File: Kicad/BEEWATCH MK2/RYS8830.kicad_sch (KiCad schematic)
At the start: 33 parts, among them Q4 DMG6968U, Q5 BSS138, Q6 BSS138, Q7 BSS138, Q8 DMP1045U-7, U2 LTC3549EDCB#TRMPBF, U7 RYS8830

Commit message: Changed +3V3 to +3.3V
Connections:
- net +3V3 renamed +3.3V
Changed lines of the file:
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@@
-	)
-	(symbol
-		(lib_id "power:+5V")
-		(at 228.6 100.33 0)
-		(mirror x)
-		(unit 1)
-		(exclude_from_sim no)
-		(in_bom yes)
-		(on_board yes)
-		(dnp no)
-		(property "Reference" "#PWR068"
-			(at 228.6 96.52 0)
-			(effects
-				(font
-					(size 1.27 1.27)
-				)
-				(hide yes)
-			)
-		)
-		(property "Value" "+3V3"
-			(at 228.6 105.41 0)
-			(effects
-				(font
-					(size 1.27 1.27)
-				)
-			)
-		)
-		(property "Footprint" ""
-			(at 228.6 100.33 0)
-			(effects
-				(font
-					(size 1.27 1.27)
-				)
-				(hide yes)
-			)
-		)
-		(property "Datasheet" ""
-			(at 228.6 100.33 0)
-			(effects
-				(font
-					(size 1.27 1.27)
-				)
-				(hide yes)
-			)
-		)
-		(property "Description" "Power symbol creates a global label with name \"+5V\""
-			(at 228.6 100.33 0)
-			(effects
-				(font
-					(size 1.27 1.27)
-				)
-				(hide yes)
-			)
-		)
-		(pin "1"
-		)
-		(instances
-			(project "BEEWATCH MK3"
-				(path "/e9c5fb53-480b-4989-8495-a3341ee99514/33dec73c-f7ec-4dd7-9d85-ef473e07baa9"
-					(reference "#PWR068")
-					(unit 1)
-				)
-			)
-		)
 	)
 	(symbol
@@
 	)
 	(symbol
+		(lib_id "power:+5V")
+		(at 229.87 152.4 180)
+		(unit 1)
+		(exclude_from_sim no)
+		(in_bom yes)
+		(on_board yes)
+		(dnp no)
+		(property "Reference" "#PWR087"
+			(at 229.87 148.59 0)
+			(effects
+				(font
+					(size 1.27 1.27)
+				)
+				(hide yes)
+			)
+		)
+		(property "Value" "+3.3V"
+			(at 229.87 157.48 0)
+			(effects
+				(font
+					(size 1.27 1.27)
+				)
+			)
+		)
+		(property "Footprint" ""
+			(at 229.87 152.4 0)
+			(effects
+				(font
+					(size 1.27 1.27)
+				)
+				(hide yes)
+			)
+		)
+		(property "Datasheet" ""
+			(at 229.87 152.4 0)
+			(effects
+				(font
+					(size 1.27 1.27)
+				)
+				(hide yes)
+			)
+		)
+		(property "Description" "Power symbol creates a global label with name \"+5V\""
+			(at 229.87 152.4 0)
+			(effects
+				(font
+					(size 1.27 1.27)
+				)
+				(hide yes)
+			)
+		)
+		(pin "1"
+		)
+		(instances
+			(project "BEEWATCH MK2"
+				(path "/e9c5fb53-480b-4989-8495-a3341ee99514/33dec73c-f7ec-4dd7-9d85-ef473e07baa9"
+					(reference "#PWR087")
+					(unit 1)
+				)
+			)
+		)
+	)
+	(symbol
 		(lib_id "Device:C_Small")
 		(at 30.48 85.09 0)
@@
 	)
 	(symbol
-		(lib_id "power:+5V")
-		(at 229.87 152.4 0)
-		(mirror x)
-		(unit 1)
-		(exclude_from_sim no)
-		(in_bom yes)
-		(on_board yes)
-		(dnp no)
-		(property "Reference" "#PWR069"
-			(at 229.87 148.59 0)
-			(effects
-				(font
-					(size 1.27 1.27)
-				)
-				(hide yes)
-			)
-		)
-		(property "Value" "+3V3"
-			(at 229.87 157.48 0)
-			(effects
-				(font
-					(size 1.27 1.27)
-				)
-			)
-		)
-		(property "Footprint" ""
-			(at 229.87 152.4 0)
-			(effects
-				(font
-					(size 1.27 1.27)
-				)
-				(hide yes)
-			)
-		)
-		(property "Datasheet" ""
-			(at 229.87 152.4 0)
-			(effects
-				(font
-					(size 1.27 1.27)
-				)
-				(hide yes)
-			)
-		)
-		(property "Description" "Power symbol creates a global label with name \"+5V\""
-			(at 229.87 152.4 0)
-			(effects
-				(font
-					(size 1.27 1.27)
-				)
-				(hide yes)
-			)
-		)
-		(pin "1"
-		)
-		(instances
-			(project "BEEWATCH MK3"
-				(path "/e9c5fb53-480b-4989-8495-a3341ee99514/33dec73c-f7ec-4dd7-9d85-ef473e07baa9"
-					(reference "#PWR069")
-					(unit 1)
-				)
-			)
-		)
-	)
-	(symbol
 		(lib_id "Transistor_FET:BSS138")
 		(at 220.98 138.43 270)
@@
 	(symbol
 		(lib_id "power:+5V")
+		(at 228.6 100.33 180)
+		(unit 1)
+		(exclude_from_sim no)
+		(in_bom yes)
+		(on_board yes)
+		(dnp no)
+		(property "Reference" "#PWR086"
+			(at 228.6 96.52 0)
+			(effects
+				(font
+					(size 1.27 1.27)
+				)
+				(hide yes)
+			)
+		)
+		(property "Value" "+3.3V"
+			(at 228.6 105.41 0)
+			(effects
+				(font
+					(size 1.27 1.27)
+				)
+			)
+		)
+		(property "Footprint" ""
+			(at 228.6 100.33 0)
+			(effects
+				(font
+					(size 1.27 1.27)
+				)
+				(hide yes)
+			)
+		)
+		(property "Datasheet" ""
+			(at 228.6 100.33 0)
+			(effects
+				(font
+					(size 1.27 1.27)
+				)
+				(hide yes)
+			)
+		)
+		(property "Description" "Power symbol creates a global label with name \"+5V\""
+			(at 228.6 100.33 0)
+			(effects
+				(font
+					(size 1.27 1.27)
+				)
+				(hide yes)
+			)
+		)
+		(pin "1"
+		)
+		(instances
+			(project "BEEWATCH MK2"
+				(path "/e9c5fb53-480b-4989-8495-a3341ee99514/33dec73c-f7ec-4dd7-9d85-ef473e07baa9"
+					(reference "#PWR086")
+					(unit 1)
+				)
+			)
+		)
+	)
+	(symbol
+		(lib_id "power:+5V")
 		(at 228.6 43.18 0)
 		(unit 1)
@@
 			)
 		)
-		(property "Value" "+3V3"
+		(property "Value" "+3.3V"
 			(at 228.6 38.1 0)
 			(effects
@@
 	)
 	(symbol
-		(lib_id "power:+5V")
-		(at 237.49 106.68 0)
-		(mirror y)
-		(unit 1)
-		(exclude_from_sim no)
-		(in_bom yes)
-		(on_board yes)
-		(dnp no)
-		(property "Reference" "#PWR070"
-			(at 237.49 110.49 0)
-			(effects
-				(font
-					(size 1.27 1.27)
-				)
-				(hide yes)
-			)
-		)
-		(property "Value" "+3V3"
-			(at 237.49 101.6 0)
-			(effects
-				(font
-					(size 1.27 1.27)
-				)
-			)
-		)
-		(property "Footprint" ""
-			(at 237.49 106.68 0)
-			(effects
-				(font
-					(size 1.27 1.27)
-				)
-				(hide yes)
-			)
-		)
-		(property "Datasheet" ""
-			(at 237.49 106.68 0)
-			(effects
-				(font
-					(size 1.27 1.27)
-				)
-				(hide yes)
-			)
-		)
-		(property "Description" "Power symbol creates a global label with name \"+5V\""
-			(at 237.49 106.68 0)
-			(effects
-				(font
-					(size 1.27 1.27)
-				)
-				(hide yes)
-			)
-		)
-		(pin "1"
-		)
-		(instances
-			(project "BEEWATCH MK3"
-				(path "/e9c5fb53-480b-4989-8495-a3341ee99514/33dec73c-f7ec-4dd7-9d85-ef473e07baa9"
-					(reference "#PWR070")
-					(unit 1)
-				)
-			)
-		)
-	)
-	(symbol
 		(lib_id "power:+3.3V")
 		(at 62.23 151.13 0)
@@
 					(unit 1)
 				)
+			)
+		)
+	)
+	(symbol
+		(lib_id "power:+5V")
+		(at 237.49 106.68 0)
+		(unit 1)
+		(exclude_from_sim no)
+		(in_bom yes)
+		(on_board yes)
+		(dnp no)
+		(property "Reference" "#PWR085"
+			(at 237.49 110.49 0)
+			(effects
+				(font
+					(size 1.27 1.27)
+				)
+				(hide yes)
+			)
+		)
+		(property "Value" "+3.3V"
+			(at 237.49 101.6 0)
+			(effects
+				(font
+					(size 1.27 1.27)
+				)
+			)
+		)
+		(property "Footprint" ""
+			(at 237.49 106.68 0)
+			(effects
+				(font
+					(size 1.27 1.27)
+				)
+				(hide yes)
+			)
+		)
+		(property "Datasheet" ""
+			(at 237.49 106.68 0)
+			(effects
+				(font
+					(size 1.27 1.27)
+				)
+				(hide yes)
+			)
+		)
+		(property "Description" "Power symbol creates a global label with name \"+5V\""
+			(at 237.49 106.68 0)
+			(effects
+				(font
+					(size 1.27 1.27)
+				)
+				(hide yes)
+			)
+		)
+		(pin "1"
+		)
+		(instances
+			(project "BEEWATCH MK2"
+				(path "/e9c5fb53-480b-4989-8495-a3341ee99514/33dec73c-f7ec-4dd7-9d85-ef473e07baa9"
+					(reference "#PWR085")
+					(unit 1)
+				)

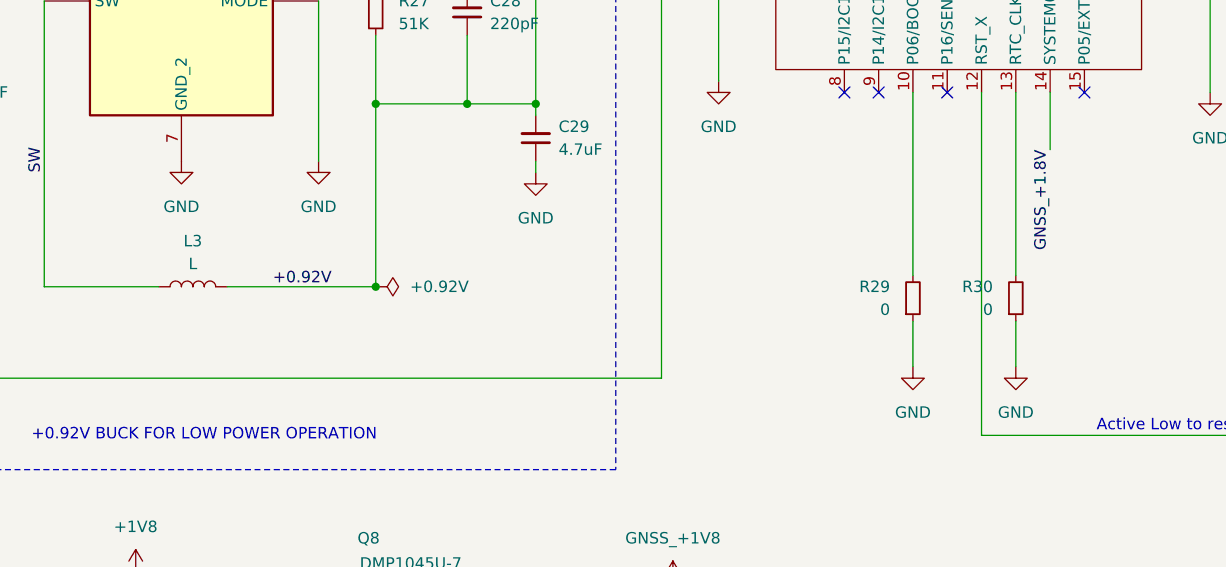
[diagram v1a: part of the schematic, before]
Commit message: Antenna and Schematic correction
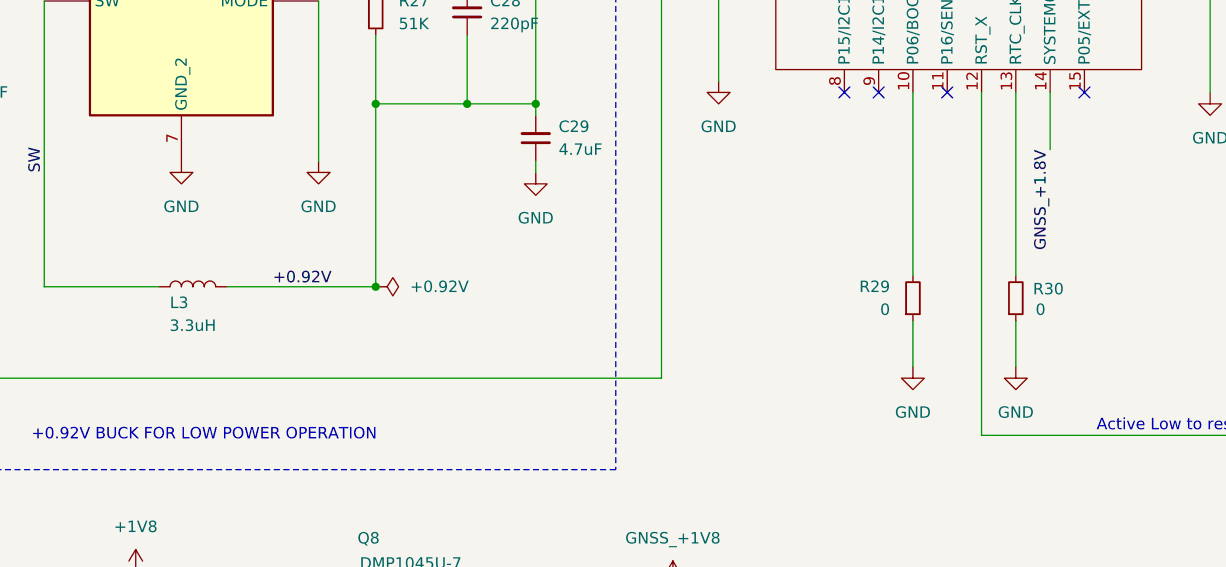
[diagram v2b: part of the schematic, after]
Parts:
- L3: value L -> 3.3uH
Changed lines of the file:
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@@
 		(on_board yes)
 		(dnp no)
-		(fields_autoplaced yes)
 		(property "Reference" "L3"
-			(at 68.58 114.3 90)
+			(at 67.056 121.158 90)
 			(effects
 				(font
@@
 			)
 		)
-		(property "Value" "L"
-			(at 68.58 116.84 90)
+		(property "Value" "3.3uH"
+			(at 68.58 123.698 90)
 			(effects
 				(font
@@
 			)
 		)
-		(property "Datasheet" "~"
+		(property "Datasheet" "https://www.sunrom.com/p/33uh-3r3-3mm-inductor"
 			(at 68.58 119.38 0)
 			(effects
@@
 		(property "Description" "Inductor"
 			(at 68.58 119.38 0)
+			(effects
+				(font
+					(size 1.27 1.27)
+				)
+				(hide yes)
+			)
+		)
+		(property "Field5" ""
+			(at 68.58 119.38 90)
 			(effects
 				(font
@@
 		(dnp no)
 		(property "Reference" "R30"
-			(at 157.48 119.3799 0)
+			(at 165.354 119.634 0)
 			(effects
 				(font
@@
 		)
 		(property "Value" "0"
-			(at 157.48 121.9199 0)
+			(at 163.322 121.92 0)
 			(effects
 				(font

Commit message: Hope this by next week gerbers will generate
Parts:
- U2: footprint Package_DFN_QFN:DFN-6-1EP_3x2mm_P0.5mm_EP1.65x1.35mm -> SM_BUCK:SON50P300X200X80-7N-D
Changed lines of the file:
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@@
 			)
 		)
-		(property "Footprint" "Package_DFN_QFN:DFN-6-1EP_3x2mm_P0.5mm_EP1.65x1.35mm"
+		(property "Footprint" "SM_BUCK:SON50P300X200X80-7N-D"
 			(at 66.04 80.01 0)
 			(effects

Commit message: DFM
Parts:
- L3: MPN (none) -> NRH2410T3R3MN

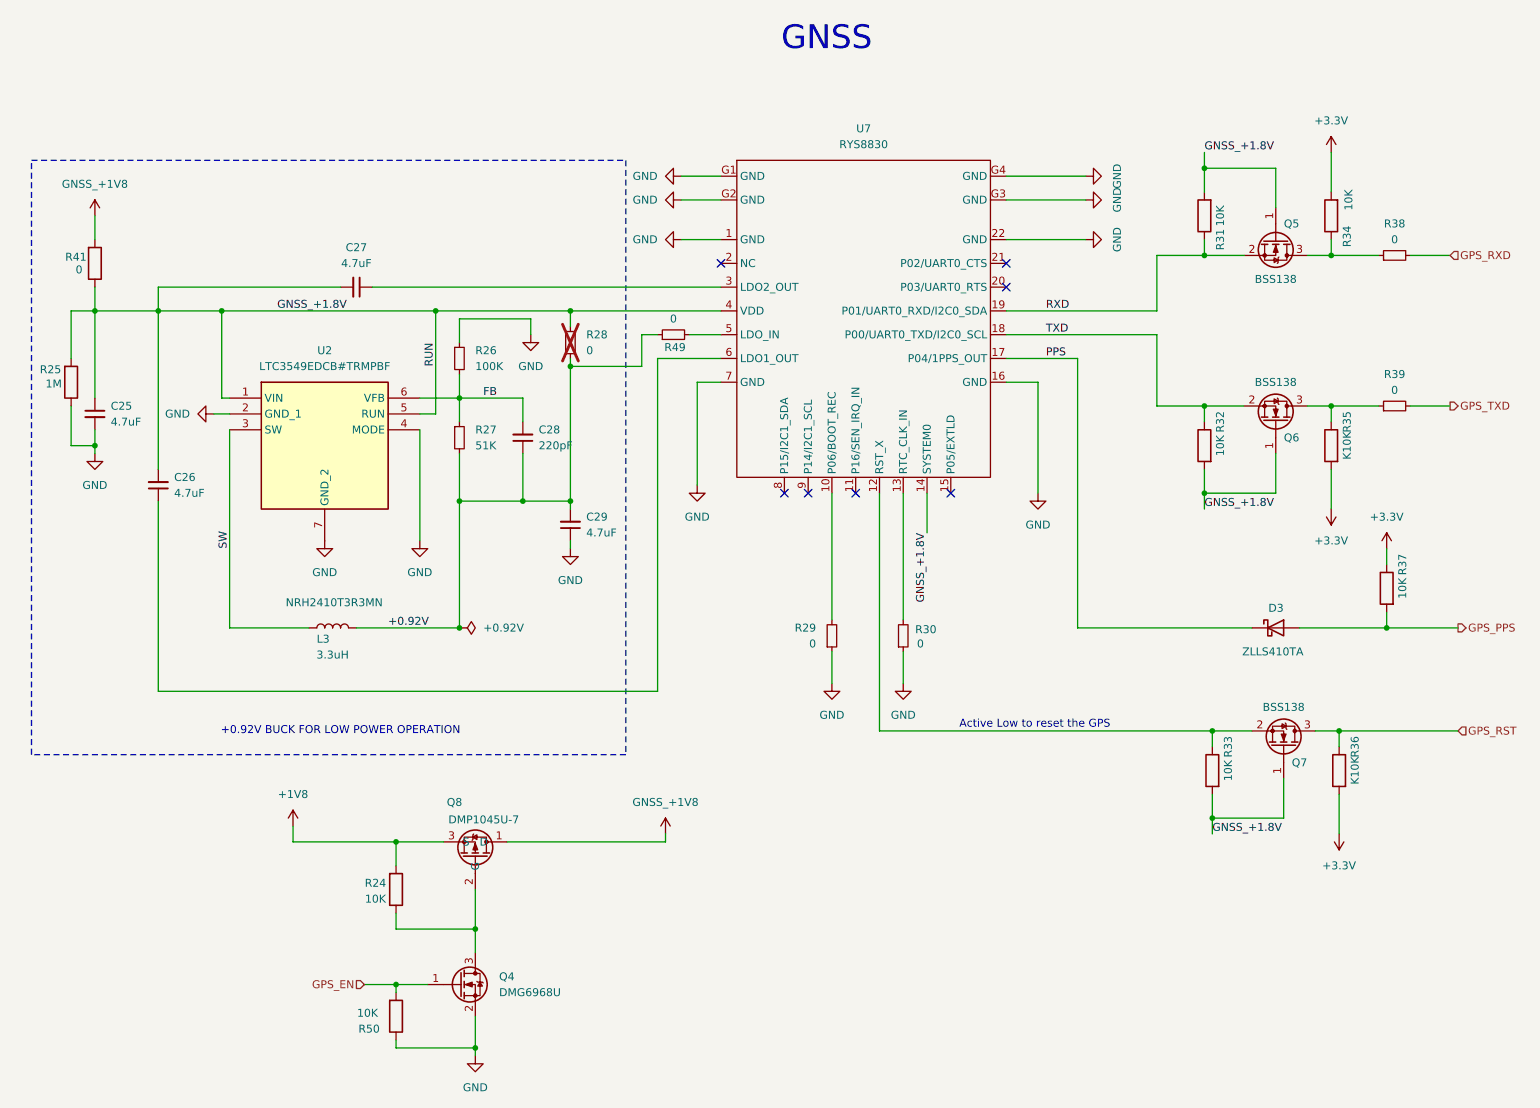
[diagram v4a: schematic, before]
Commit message: Updating MPN
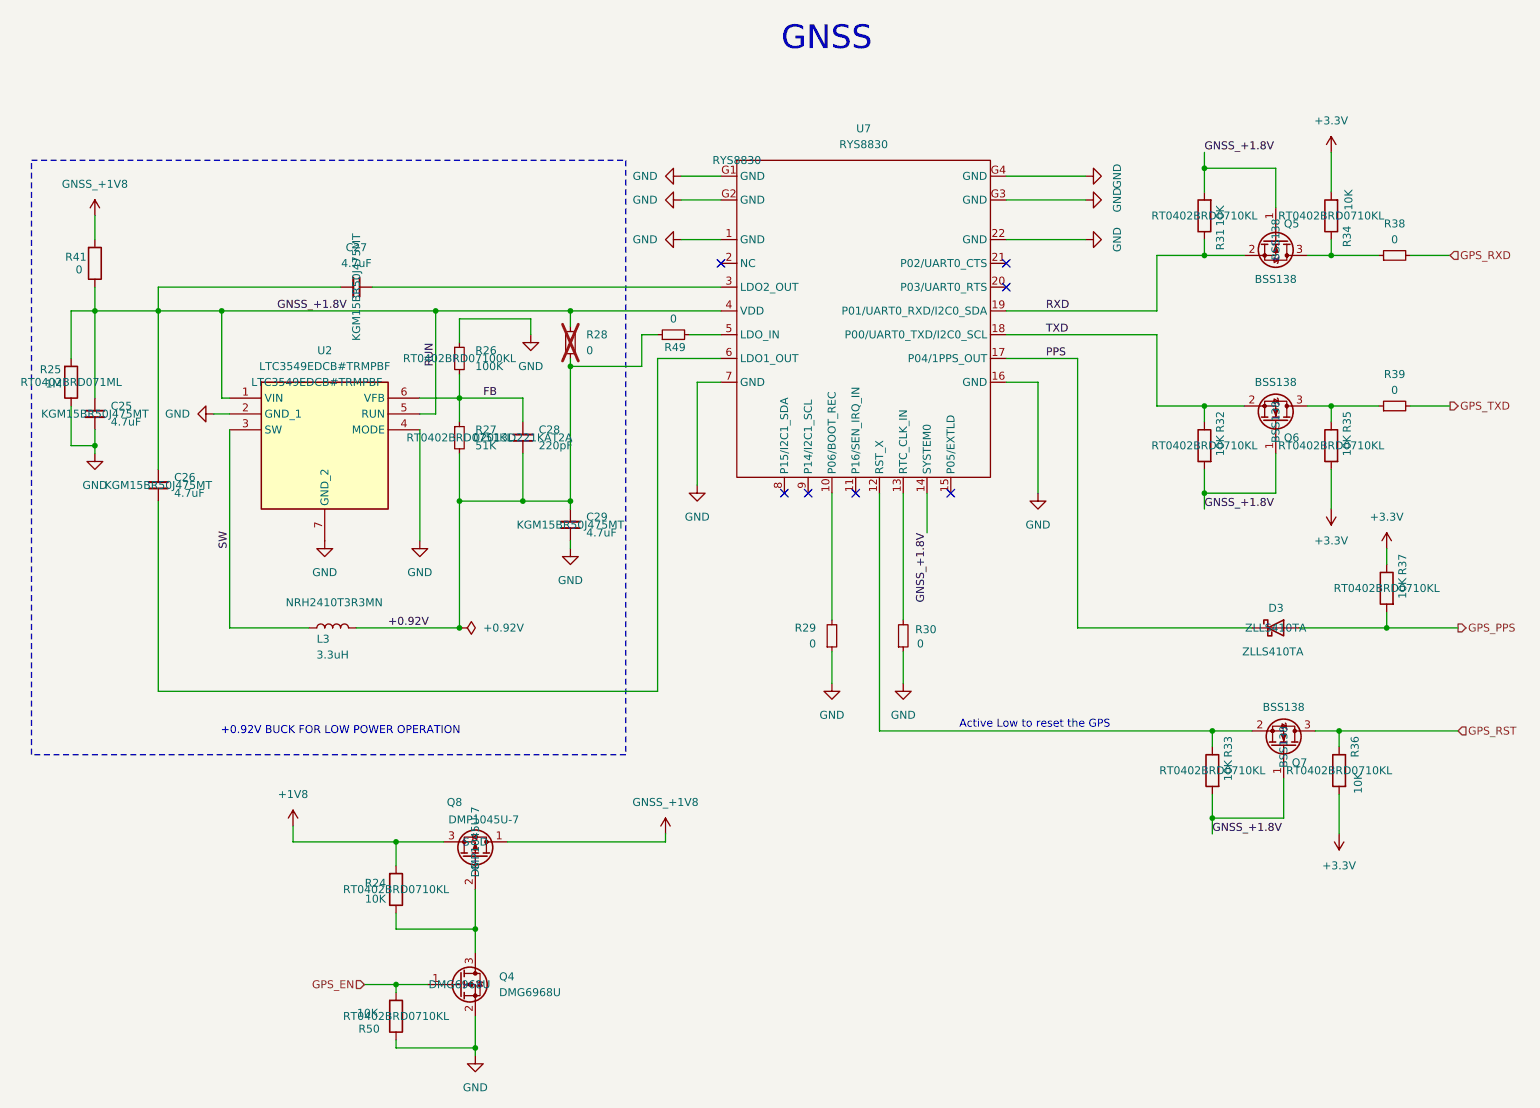
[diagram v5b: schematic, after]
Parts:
- C25, C26, C27, C29: MPN (none) -> KGM15BR50J475MT
- C28: MPN (none) -> 02013D221KAT2A
- D3: MPN (none) -> ZLLS410TA
- Q4: MPN (none) -> DMG6968U
- Q5, Q6, Q7: MPN (none) -> BSS138
- Q8: MPN (none) -> DMP1045U-7
- R24, R31, R32, R33, R34, R37, R50: MPN (none) -> RT0402BRD0710KL
- R25: MPN (none) -> RT0402BRD071ML
- R26: MPN (none) -> RT0402BRD07100KL
- R27: MPN (none) -> RT0402BRD0751KL
- R35, R36: value K10K -> 10K; MPN (none) -> RT0402BRD0710KL
- U2: MPN (none) -> LTC3549EDCB#TRMPBF
- U7: MPN (none) -> RYS8830
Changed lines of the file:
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@@
 			)
 		)
-		(property "MPN" ""
+		(property "MPN" "RT0402BRD0710KL "
 			(at 208.28 53.34 0)
 			(effects
@@
 			)
 		)
-		(property "MPN" ""
+		(property "MPN" "BSS138"
 			(at 219.71 57.15 0)
 			(effects
@@
 			)
 		)
-		(property "MPN" ""
+		(property "MPN" "DMP1045U-7"
 			(at 91.44 153.67 0)
 			(effects
@@
 			)
 		)
-		(property "MPN" ""
+		(property "MPN" "KGM15BR50J475MT "
 			(at 40.64 96.52 0)
 			(effects
@@
 			)
 		)
-		(property "Value" "K10K"
+		(property "Value" "10K"
 			(at 231.14 90.17 90)
 			(effects
@@
 			)
 		)
-		(property "MPN" ""
+		(property "MPN" "RT0402BRD0710KL "
 			(at 228.6 90.17 0)
 			(effects
@@
 			)
 		)
-		(property "MPN" ""
+		(property "MPN" "RYS8830"
 			(at 133.35 44.45 0)
 			(effects
@@
 			)
 		)
-		(property "MPN" ""
+		(property "MPN" "KGM15BR50J475MT "
 			(at 106.68 102.87 0)
 			(effects
@@
 			)
 		)
-		(property "MPN" ""
+		(property "MPN" "LTC3549EDCB#TRMPBF"
 			(at 66.04 80.01 0)
 			(effects
@@
 			)
 		)
-		(property "MPN" ""
+		(property "MPN" "RT0402BRD0710KL "
 			(at 208.28 90.17 0)
 			(effects
@@
 			)
 		)
-		(property "MPN" ""
+		(property "MPN" "RT0402BRD0710KL "
 			(at 78.74 161.29 0)
 			(effects
@@
 			)
 		)
-		(property "MPN" ""
+		(property "MPN" "DMG6968U"
 			(at 88.9 176.53 0)
 			(effects
@@
 			)
 		)
-		(property "MPN" ""
+		(property "MPN" "ZLLS410TA"
 			(at 219.71 119.38 0)
 			(effects
@@
 			)
 		)
-		(property "MPN" ""
+		(property "MPN" "KGM15BR50J475MT "
 			(at 30.48 85.09 0)
 			(effects
@@
 			)
 		)
-		(property "MPN" ""
+		(property "MPN" "RT0402BRD0710KL "
 			(at 78.74 181.61 0)
 			(effects
@@
 			)
 		)
-		(property "MPN" ""
+		(property "MPN" "BSS138"
 			(at 220.98 138.43 0)
 			(effects
@@
 			)
 		)
-		(property "MPN" ""
+		(property "MPN" "KGM15BR50J475MT "
 			(at 72.39 64.77 0)
 			(effects
@@
 			)
 		)
-		(property "MPN" ""
+		(property "MPN" "RT0402BRD0710KL "
 			(at 237.49 113.03 0)
 			(effects
@@
 			)
 		)
-		(property "MPN" ""
+		(property "MPN" "02013D221KAT2A "
 			(at 99.06 88.9 0)
 			(effects
@@
 			)
 		)
-		(property "MPN" ""
+		(property "MPN" "RT0402BRD0710KL "
 			(at 228.6 53.34 0)
 			(effects
@@
 			)
 		)
-		(property "MPN" ""
+		(property "MPN" "RT0402BRD0710KL "
 			(at 209.55 142.24 0)
 			(effects
@@
 			)
 		)
-		(property "MPN" ""
+		(property "MPN" "RT0402BRD0751KL "
 			(at 88.9 88.9 0)
 			(effects
@@
 			)
 		)
-		(property "MPN" ""
+		(property "MPN" "RT0402BRD071ML "
 			(at 26.67 80.01 0)
 			(effects
@@
 			)
 		)
-		(property "MPN" ""
+		(property "MPN" "RT0402BRD07100KL"
 			(at 88.9 76.2 0)
 			(effects
@@
 			)
 		)
-		(property "MPN" ""
+		(property "MPN" "BSS138"
 			(at 219.71 86.36 0)
 			(effects
@@
 			)
 		)
-		(property "Value" "K10K"
-			(at 232.41 142.24 90)
+		(property "Value" "10K"
+			(at 232.918 144.272 90)
 			(effects
 				(font
@@
 			)
 		)
-		(property "MPN" ""
+		(property "MPN" "RT0402BRD0710KL "
 			(at 229.87 142.24 0)
 			(effects
